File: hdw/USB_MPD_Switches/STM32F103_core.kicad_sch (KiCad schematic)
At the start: 27 parts

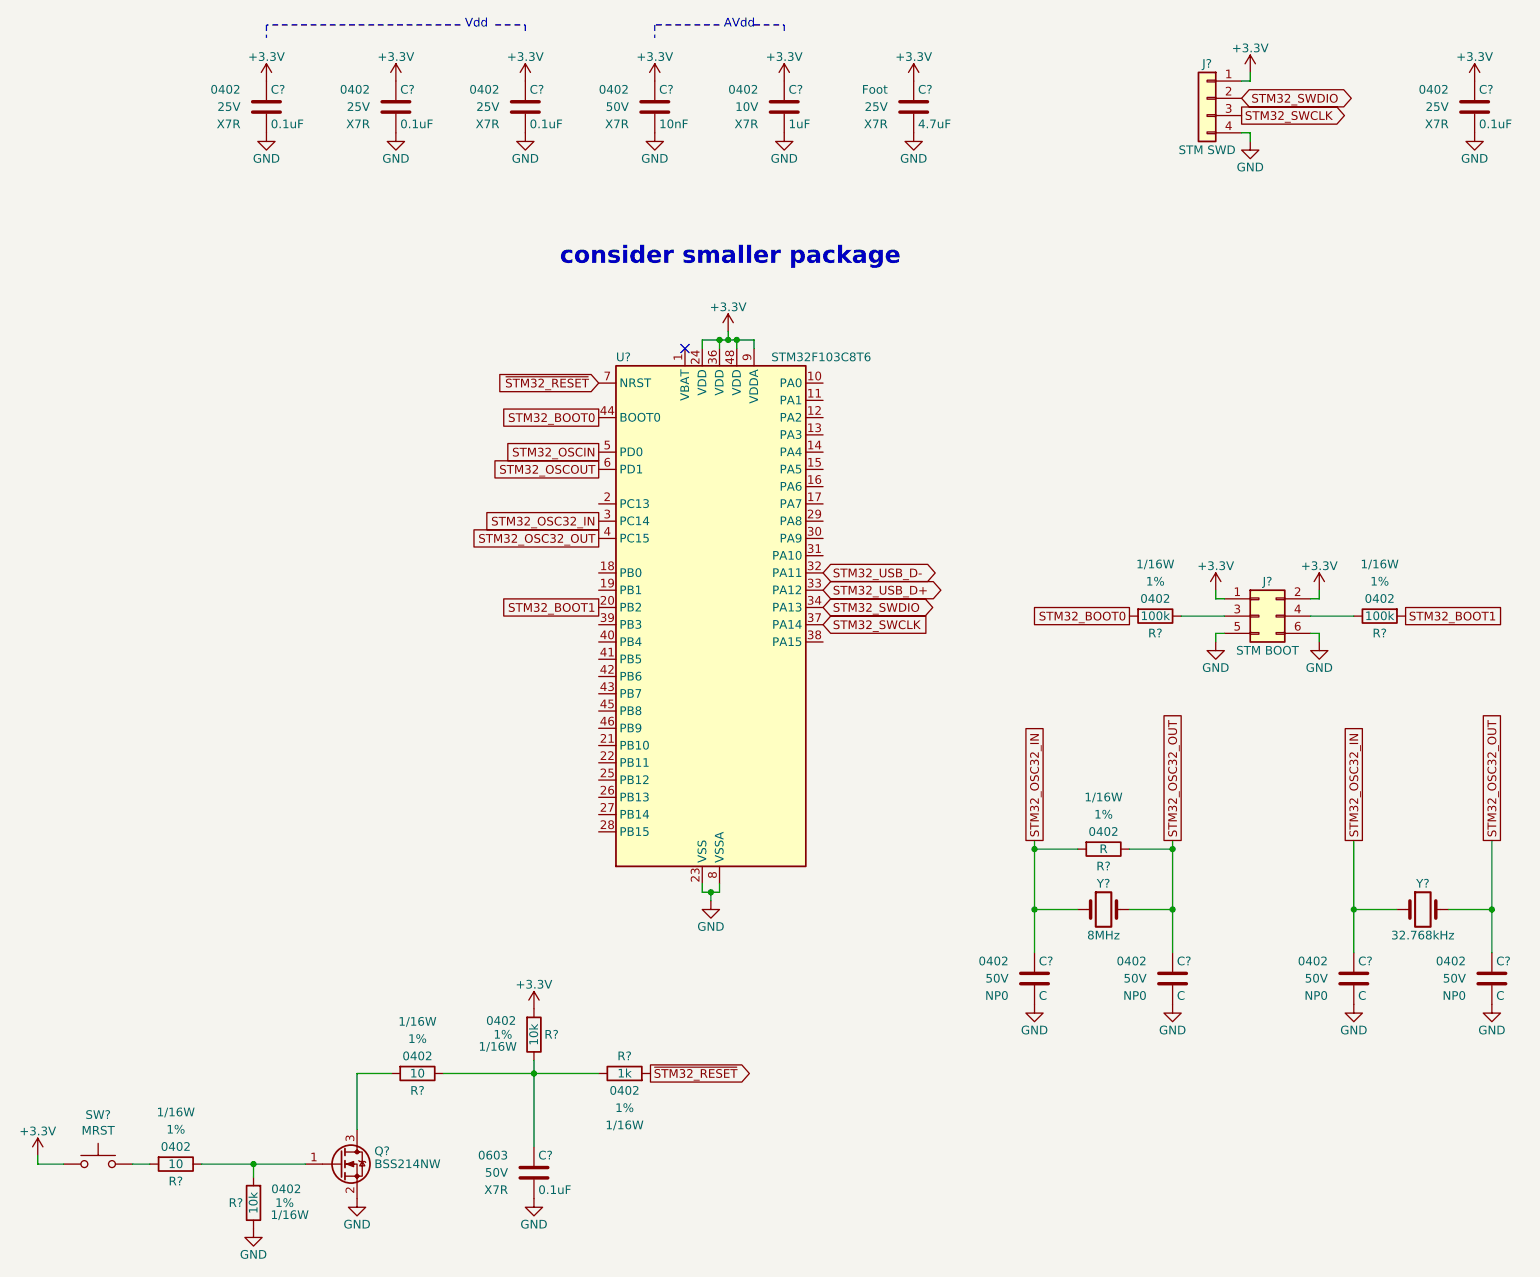
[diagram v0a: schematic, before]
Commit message: added USB port, +3.3V power supply
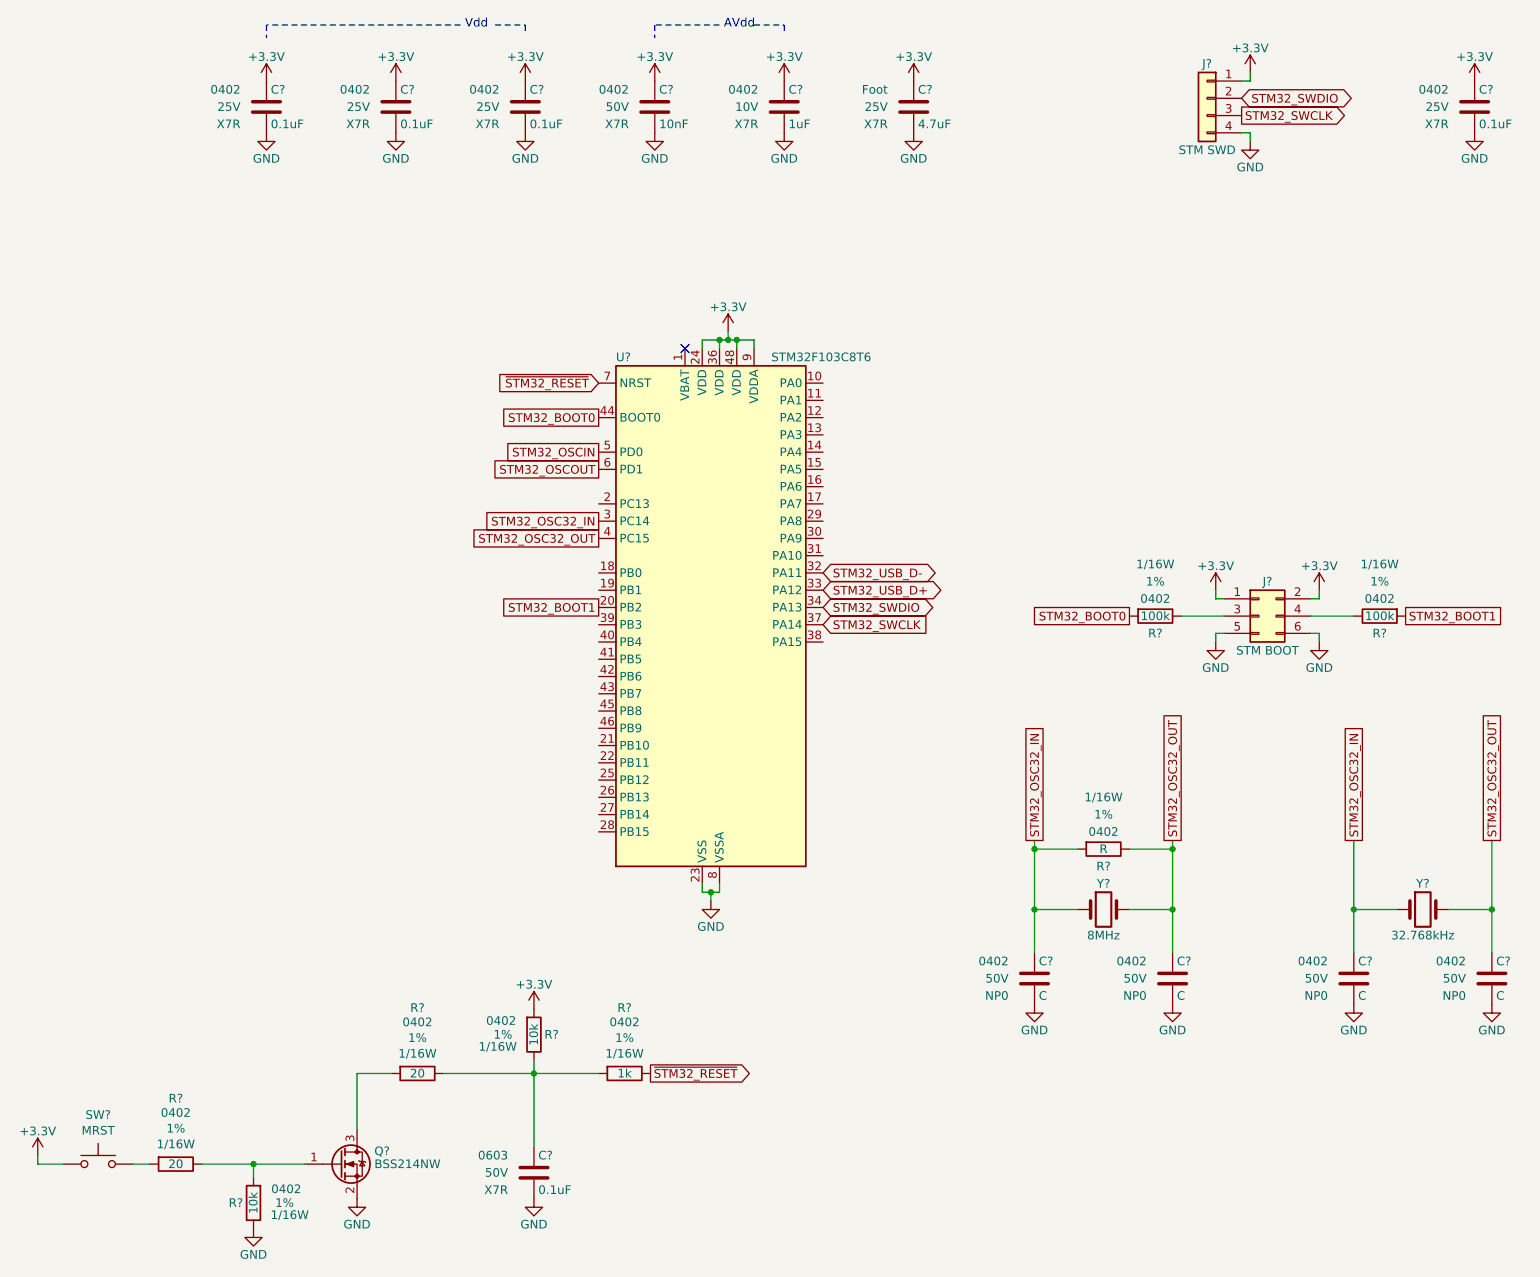
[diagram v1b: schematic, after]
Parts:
- removed R? (x2): 10, symbol Custom_Library:R_Custom
- removed R?: 1k, symbol Custom_Library:R_Custom
- added R?: 1k, Resistors_SMD:R_0402, symbol Custom_Library:R_Custom
- added R? (x2): 20, Resistors_SMD:R_0402, symbol Custom_Library:R_Custom
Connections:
- net ~{STM32_RESET}: now also R?.2
- net at Q?.1 (G), R?.1: now also R?.2
- net at Q?.3 (D): now also R?.1
- net at C?.1, R?.2: now also R?.1, R?.2
- net at SW?.2: now also R?.1
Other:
- note removed: "consider smaller package"
